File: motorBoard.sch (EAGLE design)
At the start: 20 parts, among them IC1 PIC18F4XK22PT

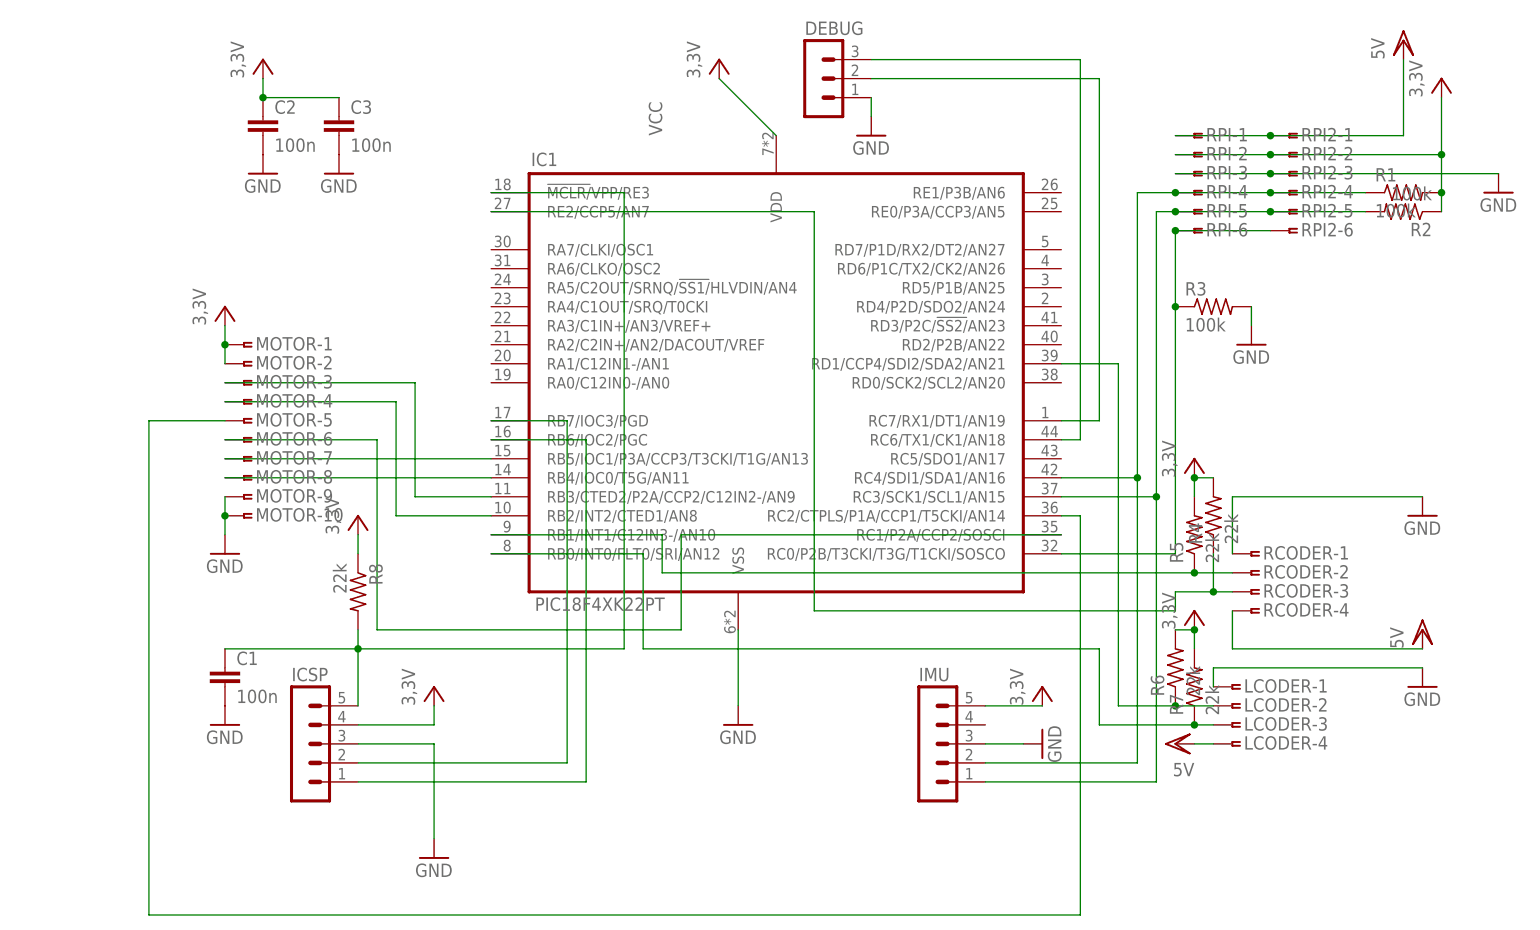
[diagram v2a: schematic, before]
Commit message: added power and status LEDs, fixed silkscreen
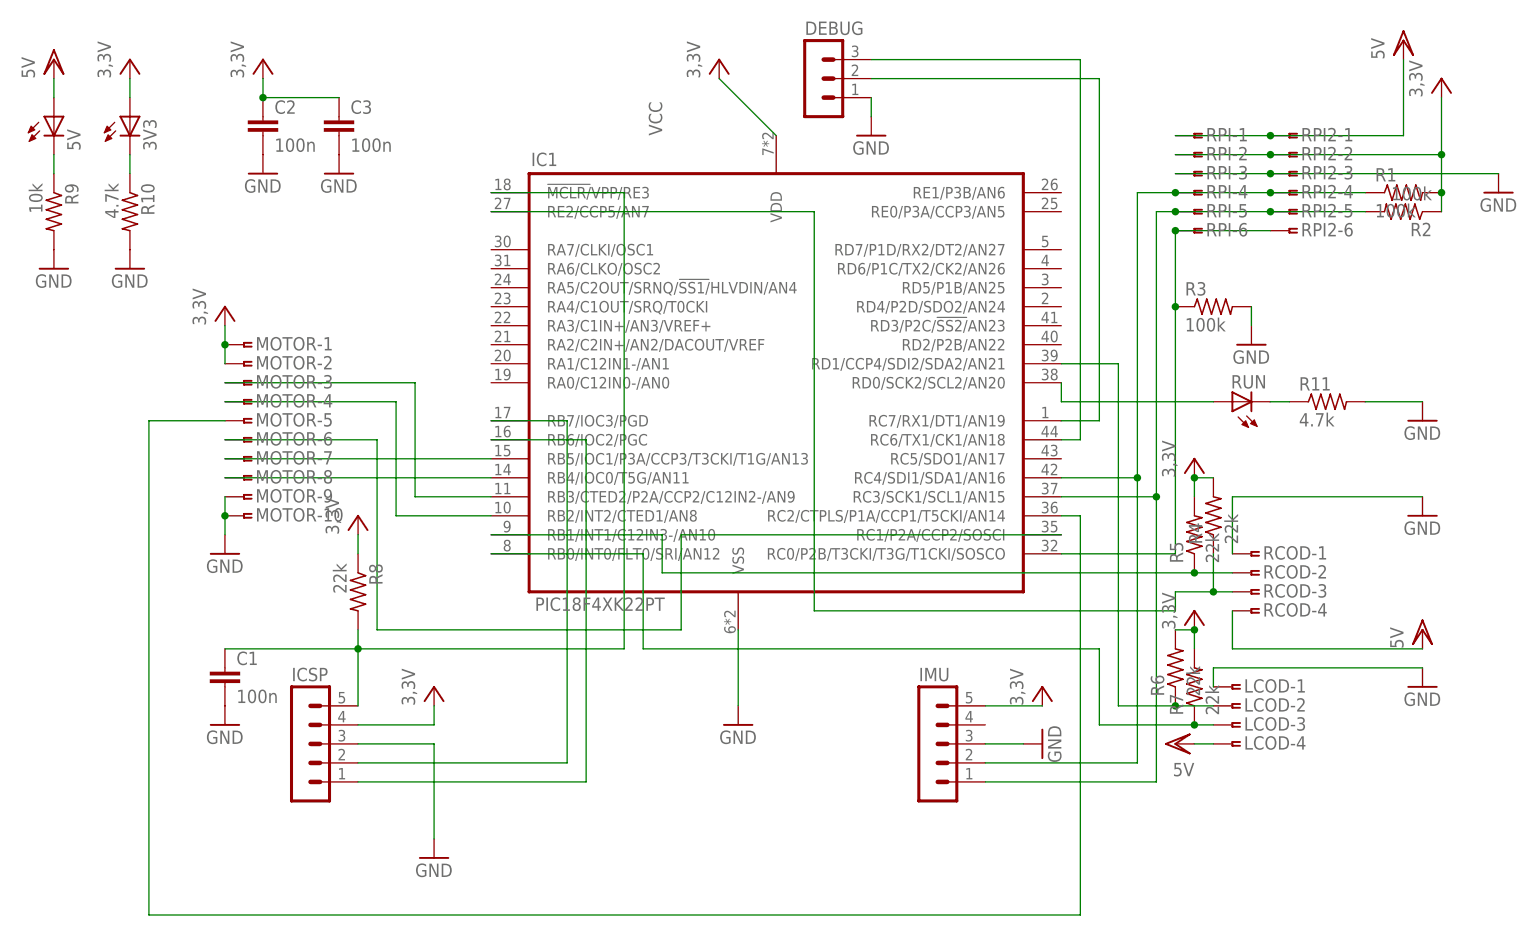
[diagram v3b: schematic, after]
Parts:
- added 3V3, 5V, RUN: (no value), adafruit:LEDCHIPLED_0805
- added R10, R11: 4.7k, resistor:R-US_M0805
- added R9: 10k, resistor:R-US_M0805
- renumbered LCODER to LCOD, RCODER to RCOD
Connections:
- new net N$10: 5V.C, R9.1
- new net N$14: 3V3.C, R10.1
- new net N$15: IC1.RD0/SCK2/SCL2/AN20, RUN.A
- new net N$9: R11.1, RUN.C
- net GND: now also R10.2, R11.2, R9.2
- net VCC: now also 3V3.A
- net VDD: now also 5V.A
